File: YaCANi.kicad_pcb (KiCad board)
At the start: 2 copper layers, 20 x 50 mm, 65 parts, among them P1 SWD, P2 CAN, P3 USB, U1 STM32F042C6T6, U2 MCP2562-E/SN, U3 LD1117S33TR

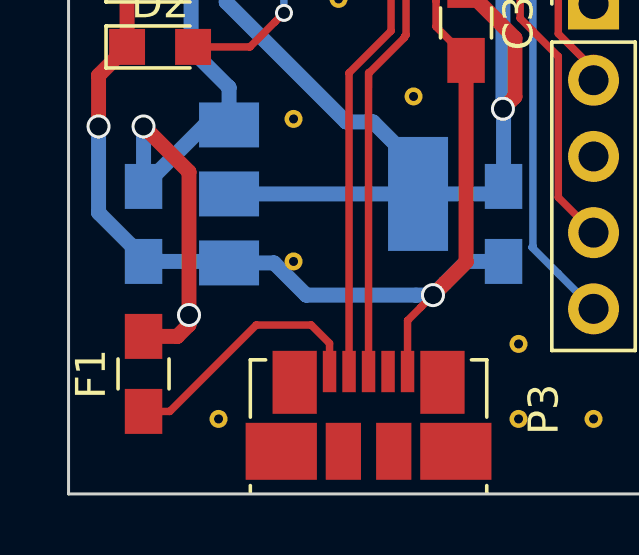
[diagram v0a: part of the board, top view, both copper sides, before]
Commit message: remove useless via
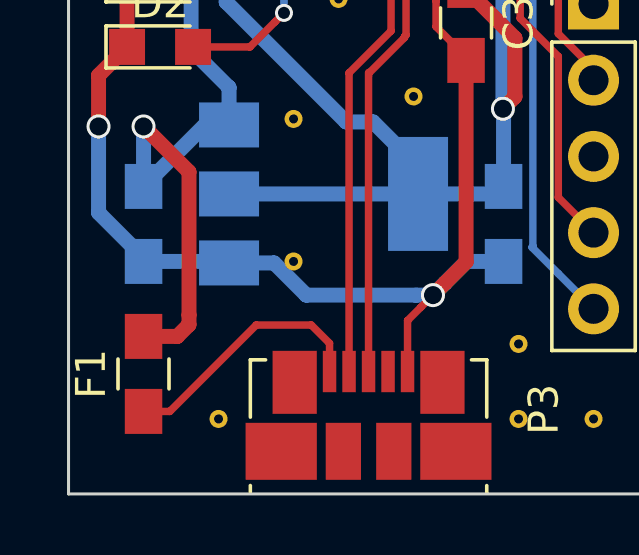
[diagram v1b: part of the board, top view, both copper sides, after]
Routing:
- net +5V: vias 3 -> 2
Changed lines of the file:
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@@
     (links 106)
     (no_connects 0)
-    (area 121.699999 77.449999 141.800001 127.550001)
+    (area 117.607142 69.8 154.6 129.315001)
     (thickness 1.6)
     (drawings 6)
-    (tracks 275)
+    (tracks 274)
     (zones 0)
     (modules 65)
@@
   (segment (start 124.25 117.25) (end 124.25 117.375) (width 0.5) (layer B.Cu) (net 2))
   (segment (start 125.375 122.25) (end 125.764927 121.860073) (width 0.5) (layer F.Cu) (net 2))
-  (via (at 125.764927 121.535567) (size 0.8) (drill 0.6) (layers F.Cu B.Cu) (net 2))
   (segment (start 133.25 95.5) (end 133.25 96.66) (width 0.5) (layer F.Cu) (net 2))
   (segment (start 133.25 96.66) (end 133.76 97.17) (width 0.5) (layer F.Cu) (net 2))

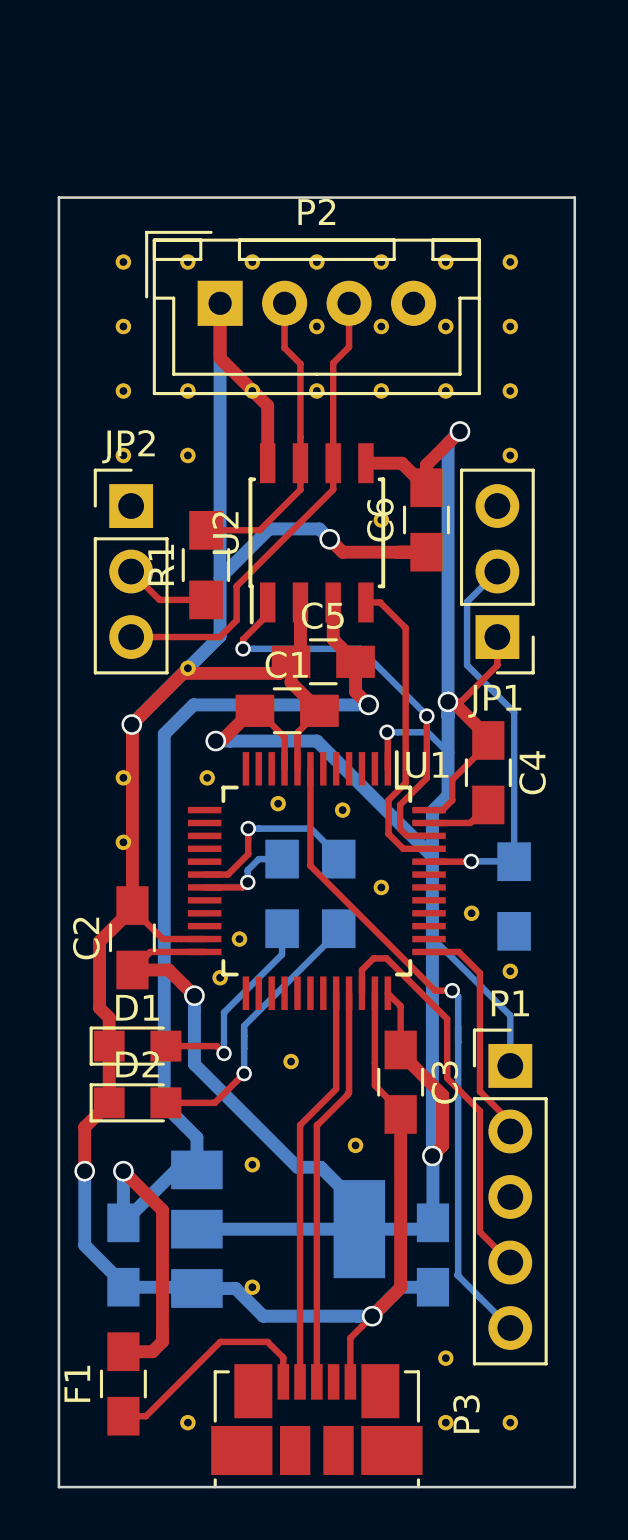
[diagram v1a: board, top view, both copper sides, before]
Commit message: change CAN connector to an angled version
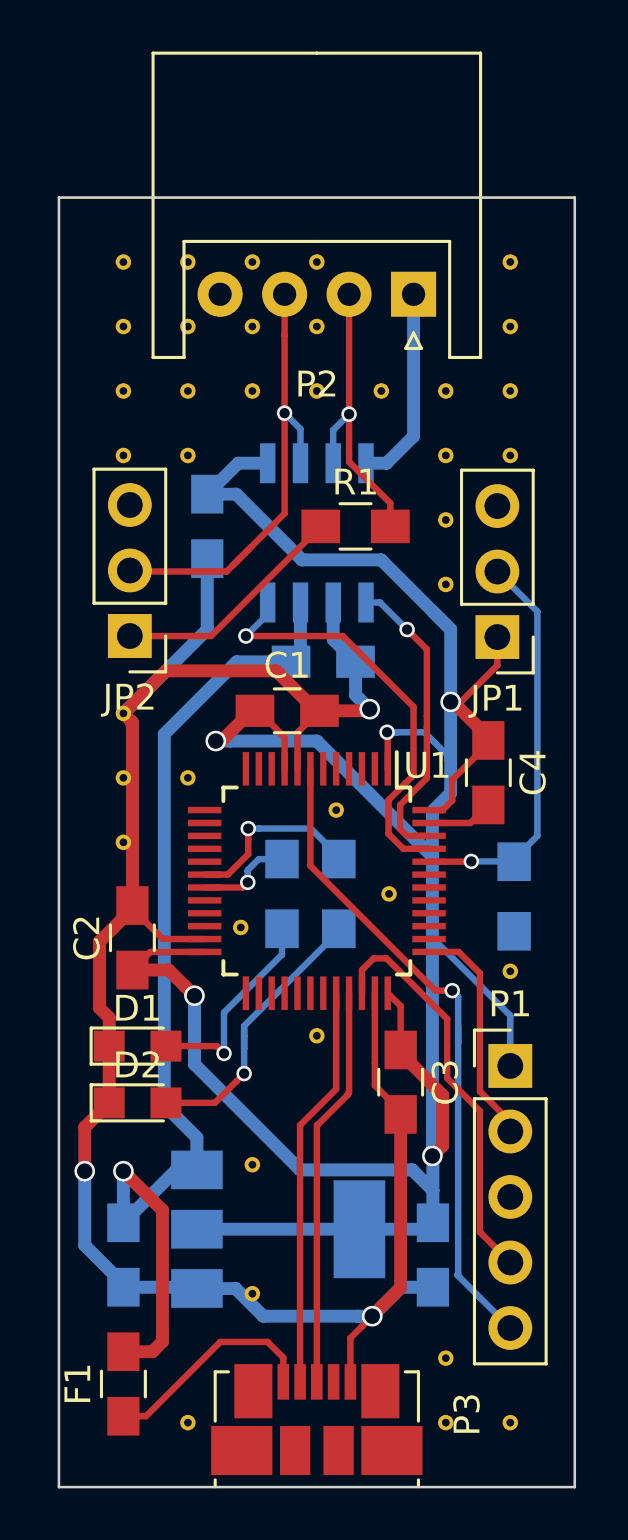
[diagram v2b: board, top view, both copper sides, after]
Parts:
- removed the REF** at (134.2, 90.0)
- removed the REF** at (136.8, 82.5)
- removed the REF** at (134.2, 82.5)
- removed the REF** at (136.8, 80.0)
- removed the REF** at (134.2, 80.0)
- removed the REF** at (127.5, 100.0)
- removed the REF** at (132.8, 101.2)
- removed the REF** at (128.0, 107.8)
- removed the REF** at (129.2, 119.8)
- removed the REF** at (133.2, 114.2)
- removed the REF** at (128.8, 106.2)
- removed the REF** at (130.2, 101.0)
- removed the REF** at (137.8, 105.2)
- removed the REF** at (126.8, 95.8)
- removed the REF** at (130.8, 111.0)
- removed the REF** at (134.2, 104.2)
- added REF**: Via, PhoenixRobotik:Via-0.6mm, F.Cu at (126.8, 100.0)
- added REF**: Via, PhoenixRobotik:Via-0.6mm, F.Cu at (124.2, 97.5)
- added REF**: Via, PhoenixRobotik:Via-0.6mm, F.Cu at (136.8, 92.5)
- added REF**: Via, PhoenixRobotik:Via-0.6mm, F.Cu at (136.8, 90.0)
- added REF**: Via, PhoenixRobotik:Via-0.6mm, F.Cu at (136.8, 87.5)
- added REF**: Via, PhoenixRobotik:Via-0.6mm, F.Cu at (129.2, 82.5)
- added REF**: Via, PhoenixRobotik:Via-0.6mm, F.Cu at (126.8, 82.5)
- added REF**: Via, PhoenixRobotik:Via-0.6mm, F.Cu at (132.5, 101.2)
- added REF**: Via, PhoenixRobotik:Via-0.6mm, F.Cu at (134.6, 104.5)
- added REF**: Via, PhoenixRobotik:Via-0.6mm, F.Cu at (129.2, 120.0)
- added REF**: Via, PhoenixRobotik:Via-0.6mm, F.Cu at (131.8, 110.0)
- added REF**: Via, PhoenixRobotik:Via-0.6mm, F.Cu at (128.8, 105.8)
- C5, C6, U2: moved to B.Cu
- P2: footprint Connectors_JST:JST_XH_B04B-XH-A_04x2.50mm_Straight -> Connectors_JST:JST_XH_S04B-XH-A_04x2.50mm_Angled
- moved C6 8.50 mm to (127.5, 90.2)
- moved P2 7.51 mm to (135.5, 81.2), turned to 180 degrees
- moved R1 5.99 mm to (133.2, 90.2), turned to 0 degrees
- moved JP2 5.04 mm to (124.5, 94.5), turned to 180 degrees
- turned C5 to 180 degrees
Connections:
- JP2 pad 1: (no net) -> Net-(JP2-Pad1)
- JP2 pad 2: Net-(JP2-Pad2) -> CAN_L
- JP2 pad 3: CAN_L -> (no net)
- R1 pad 1: Net-(JP2-Pad2) -> Net-(JP2-Pad1)
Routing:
- net Net-(JP2-Pad1): track 0.00 -> 9.16 mm
- net GND: track 108.3 -> 99.4 mm, vias 4 -> 3
- net /CAN_TX: track 16.4 -> 11.7 mm, vias 2 -> 1
- net /CAN_RX: track 12.0 -> 16.4 mm, vias 0 -> 1
- net +5V: track 45.2 -> 40.8 mm, vias 2 -> 1
- net +3V3: track 107.1 -> 110.9 mm, vias 6 -> 5
- net Net-(JP2-Pad2): track 3.36 -> 0.00 mm
- net CAN_H: track 11.8 -> 11.5 mm, vias 0 -> 1
- net CAN_L: track 18.5 -> 18.2 mm, vias 0 -> 1

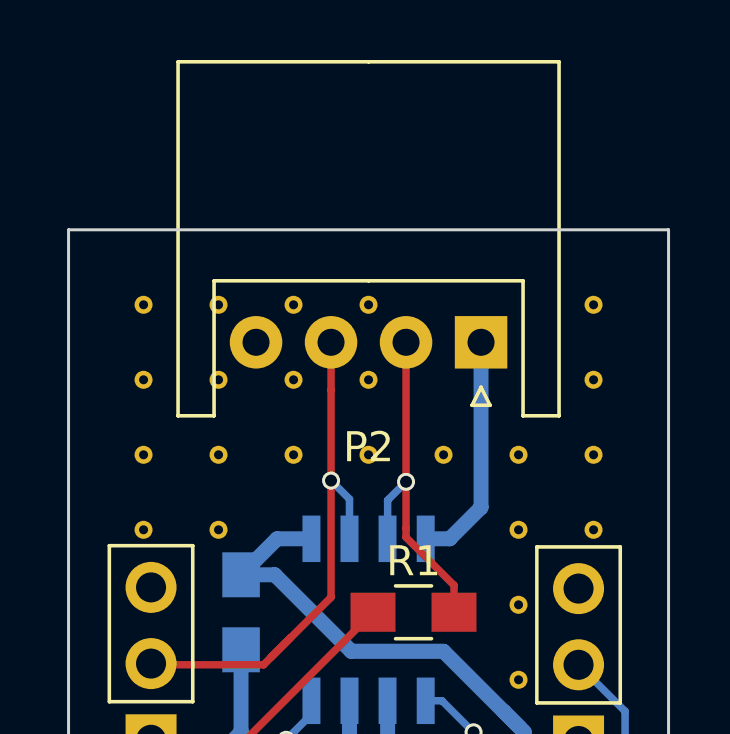
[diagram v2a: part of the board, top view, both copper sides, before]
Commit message: move CAN connector
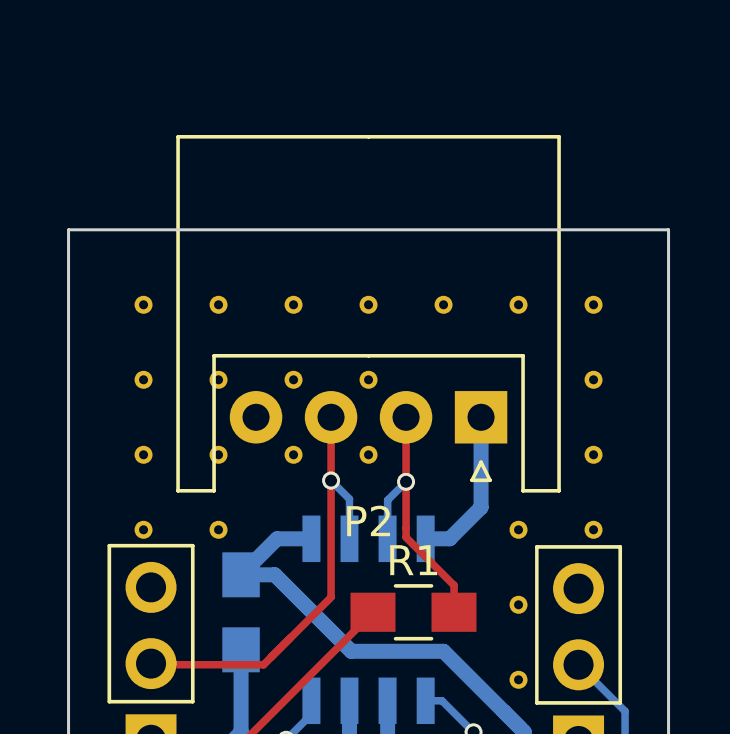
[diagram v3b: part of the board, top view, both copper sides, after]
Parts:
- moved REF** 5.00 mm to (134.2, 80.0)
- moved REF** 5.00 mm to (136.8, 80.0)
- moved P2 2.50 mm to (135.5, 83.8)
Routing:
- net GND: track 99.4 -> 97.3 mm
- net CAN_L: track 18.2 -> 16.0 mm
- net CAN_H: track 11.5 -> 9.32 mm
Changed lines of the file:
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@@
     (thickness 1.6)
     (drawings 6)
-    (tracks 279)
+    (tracks 278)
     (zones 0)
     (modules 61)
@@
   )
   (module PhoenixRobotik:Via-0.6mm (layer F.Cu)
+    (at 134.25 80)
+    (fp_text reference REF** (at 0 2) (layer F.SilkS) hide
+      (effects (font (size 1 1) (thickness 0.15)))
+    )
+    (fp_text value Via (at 0 -1.9) (layer F.Fab) hide
+      (effects (font (size 1 1) (thickness 0.15)))
+    )
+    (pad 1 thru_hole circle (at 0 0) (size 0.6 0.6) (drill 0.3) (layers *.Cu)
+      (net 1 GND) (zone_connect 2))
+  )
+  (module PhoenixRobotik:Via-0.6mm (layer F.Cu)
+    (at 136.75 80)
+    (fp_text reference REF** (at 0 2) (layer F.SilkS) hide
+      (effects (font (size 1 1) (thickness 0.15)))
+    )
+    (fp_text value Via (at 0 -1.9) (layer F.Fab) hide
+      (effects (font (size 1 1) (thickness 0.15)))
+    )
+    (pad 1 thru_hole circle (at 0 0) (size 0.6 0.6) (drill 0.3) (layers *.Cu)
+      (net 1 GND) (zone_connect 2))
+  )
+  (module PhoenixRobotik:Via-0.6mm (layer F.Cu)
     (at 139.25 125)
     (fp_text reference REF** (at 0 2) (layer F.SilkS) hide
@@
   (module PhoenixRobotik:Via-0.6mm (layer F.Cu)
     (at 139.25 85)
-    (fp_text reference REF** (at 0 2) (layer F.SilkS) hide
-      (effects (font (size 1 1) (thickness 0.15)))
-    )
-    (fp_text value Via (at 0 -1.9) (layer F.Fab) hide
-      (effects (font (size 1 1) (thickness 0.15)))
-    )
-    (pad 1 thru_hole circle (at 0 0) (size 0.6 0.6) (drill 0.3) (layers *.Cu)
-      (net 1 GND) (zone_connect 2))
-  )
-  (module PhoenixRobotik:Via-0.6mm (layer F.Cu)
-    (at 136.75 85)
-    (fp_text reference REF** (at 0 2) (layer F.SilkS) hide
-      (effects (font (size 1 1) (thickness 0.15)))
-    )
-    (fp_text value Via (at 0 -1.9) (layer F.Fab) hide
-      (effects (font (size 1 1) (thickness 0.15)))
-    )
-    (pad 1 thru_hole circle (at 0 0) (size 0.6 0.6) (drill 0.3) (layers *.Cu)
-      (net 1 GND) (zone_connect 2))
-  )
-  (module PhoenixRobotik:Via-0.6mm (layer F.Cu)
-    (at 134.25 85)
     (fp_text reference REF** (at 0 2) (layer F.SilkS) hide
       (effects (font (size 1 1) (thickness 0.15)))
@@
   )
   (module Connectors_JST:JST_XH_S04B-XH-A_04x2.50mm_Angled (layer F.Cu)
-    (at 135.5 81.25 180)
+    (at 135.5 83.75 180)
     (descr "JST XH series connector, S04B-XH-A, side entry type, through hole")
     (tags "connector jst xh tht side horizontal angled 2.50mm")
@@
     (arrow2b (pts (xy 121.75 72.5) (xy 122.876504 71.913579)))
   )
+  (segment (start 135.5 86.755) (end 135.5 83.75) (width 0.5) (layer B.Cu) (net 1))
   (segment (start 124.25 97.5) (end 127.5 94.25) (width 0.5) (layer B.Cu) (net 1))
   (segment (start 127.5 94.25) (end 127.5 94.2) (width 0.5) (layer B.Cu) (net 1))
@@
   (segment (start 130.302073 95.977073) (end 131.725 97.4) (width 0.5) (layer F.Cu) (net 1))
   (segment (start 131.725 97.4) (end 131.85 97.4) (width 0.5) (layer F.Cu) (net 1))
-  (segment (start 135.5 81.6) (end 135.5 86.755) (width 0.5) (layer B.Cu) (net 1))
   (segment (start 135.5 86.755) (end 134.455 87.8) (width 0.5) (layer B.Cu) (net 1))
   (segment (start 134.455 87.8) (end 133.655 87.8) (width 0.5) (layer B.Cu) (net 1))
@@
   (segment (start 137.73 103.25) (end 137.74 103.24) (width 0.25) (layer F.Cu) (net 14))
   (via (at 137.74 103.24) (size 0.6) (drill 0.4) (layers F.Cu B.Cu) (net 14))
+  (segment (start 130.5 85.86) (end 130.5 83.75) (width 0.25) (layer F.Cu) (net 15))
   (segment (start 128.25 92) (end 128.5 91.75) (width 0.25) (layer F.Cu) (net 15))
   (segment (start 130.5 89.75) (end 128.5 91.75) (width 0.25) (layer F.Cu) (net 15))
@@
   (segment (start 130.5 85.86) (end 131.115 86.475) (width 0.25) (layer B.Cu) (net 15))
   (segment (start 131.115 86.475) (end 131.115 87.8) (width 0.25) (layer B.Cu) (net 15))
-  (segment (start 130.5 85.86) (end 130.5 82.837436) (width 0.25) (layer F.Cu) (net 15))
   (via (at 130.5 85.86) (size 0.6) (drill 0.4) (layers F.Cu B.Cu) (net 15))
-  (segment (start 130.5 82.837436) (end 130.5 81.6) (width 0.25) (layer F.Cu) (net 15))
+  (segment (start 133 85.9) (end 133 83.75) (width 0.25) (layer F.Cu) (net 16))
   (segment (start 133 85.9) (end 133 87.45) (width 0.25) (layer F.Cu) (net 16))
   (segment (start 134.6 90.25) (end 134.6 89.35) (width 0.25) (layer F.Cu) (net 16))
@@
   (segment (start 133 85.9) (end 132.385 86.515) (width 0.25) (layer B.Cu) (net 16))
   (segment (start 132.385 86.515) (end 132.385 87.8) (width 0.25) (layer B.Cu) (net 16))
-  (segment (start 133 81.6) (end 133 85.9) (width 0.25) (layer F.Cu) (net 16))
   (via (at 133 85.9) (size 0.6) (drill 0.4) (layers F.Cu B.Cu) (net 16))
   (segment (start 129.071987 103.627404) (end 129.071987 104.051668) (width 0.25) (layer B.Cu) (net 17))

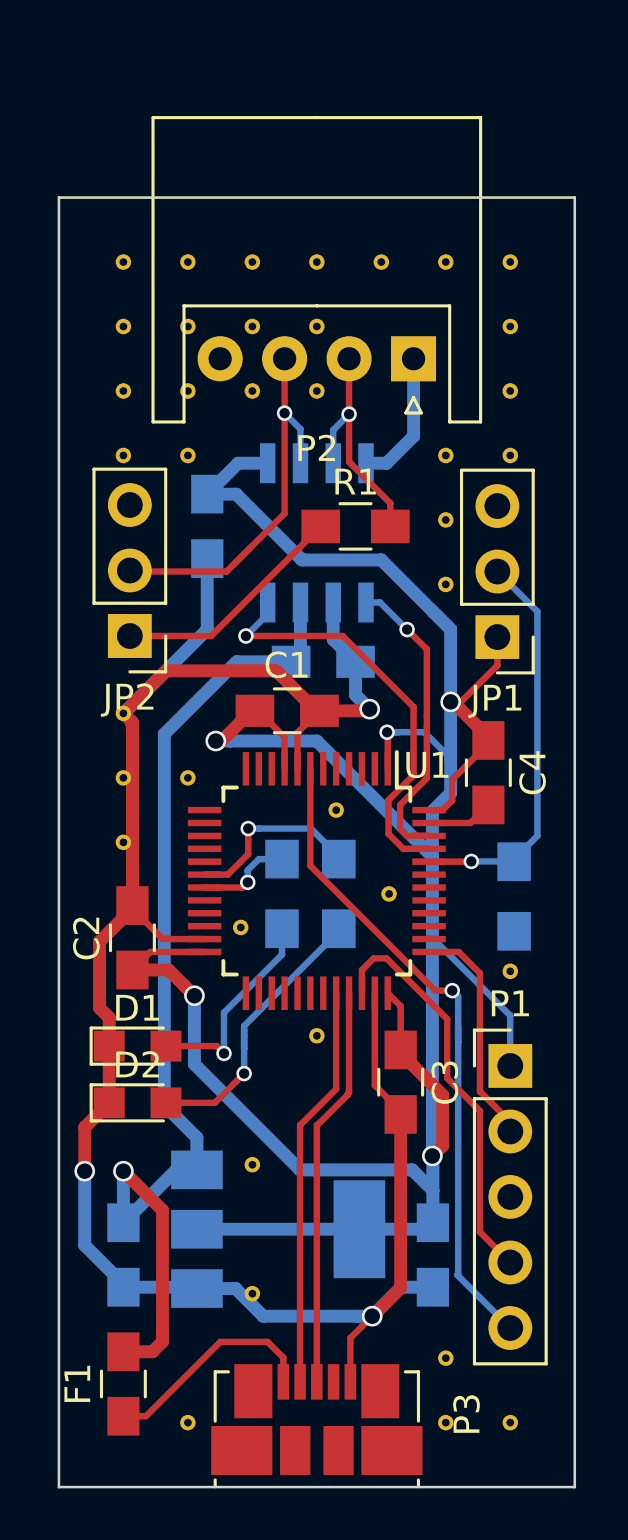
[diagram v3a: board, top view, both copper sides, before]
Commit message: add text on board
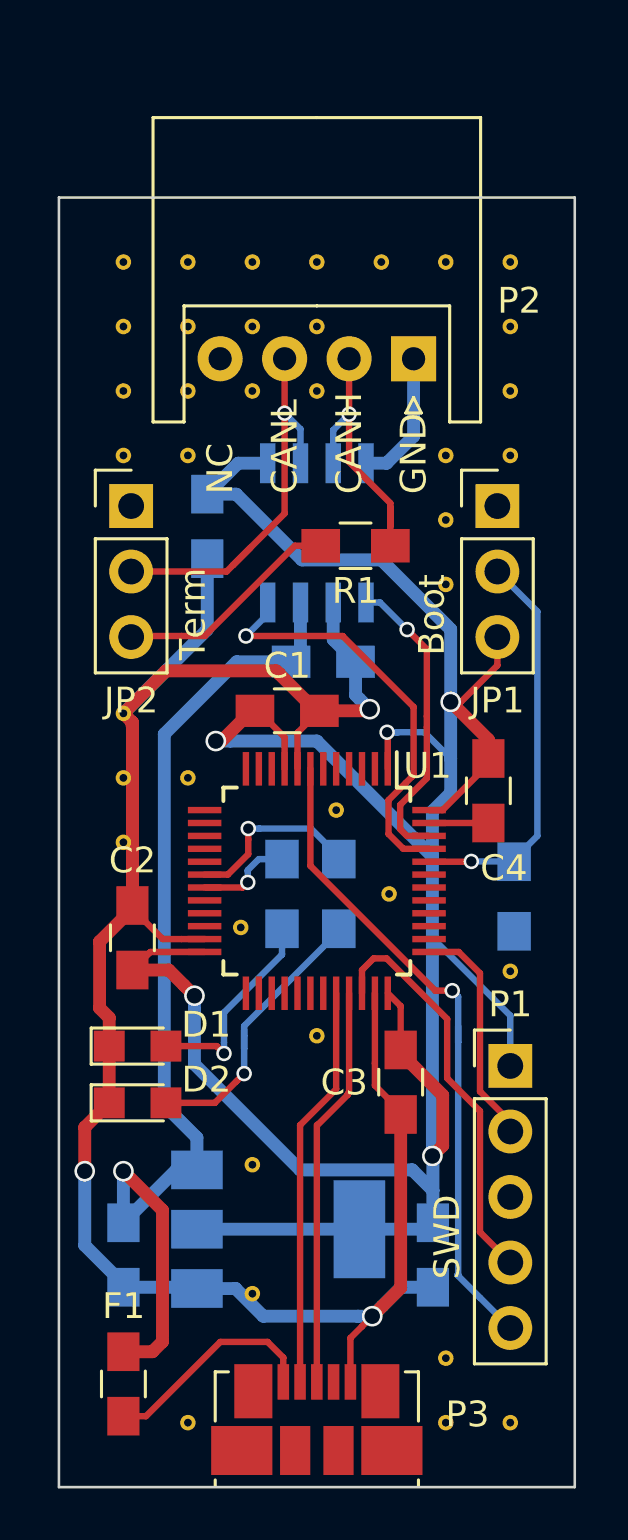
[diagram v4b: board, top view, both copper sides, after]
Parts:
- moved JP1 5.08 mm to (138.8, 89.5), turned to 0 degrees
- moved JP2 5.04 mm to (124.5, 89.5), turned to 0 degrees
- moved R1 0.75 mm to (133.2, 91.0)
- moved C4 0.70 mm to (138.4, 100.5)
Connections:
- JP1 pad 1: +3V3 -> (no net)
- JP1 pad 3: (no net) -> +3V3
- JP2 pad 1: Net-(JP2-Pad1) -> (no net)
- JP2 pad 3: (no net) -> Net-(JP2-Pad3)
- R1 pad 1: Net-(JP2-Pad1) -> Net-(JP2-Pad3)
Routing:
- net Net-(JP2-Pad1): track 9.16 -> 0.00 mm
- net Net-(JP2-Pad3): track 0.00 -> 8.85 mm
- net CAN_H: track 9.32 -> 10.8 mm
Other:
- board text added: "1. 3.3v 2. SWCLK 3. GND 4. SWDIO 5. NRST"
- board text added: "Boot"
- board text added: "CANH"
- board text added: "CANL"
- board text added: "GND"
- board text added: "NC"
- board text added: "SWD"
- board text added: "Term"

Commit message: add logo and referencies
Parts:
- added REF***: OSHW-Logo2_7.3x6mm_SilkScreen, Symbols:OSHW-Logo2_7.3x6mm_SilkScreen, F.Cu at (130.8, 115.4)
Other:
- board text added: "YaCANi"
- board text added: "github/PhoenixRobotik/YaCANi"
